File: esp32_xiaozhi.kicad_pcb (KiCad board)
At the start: 2 copper layers, 99.1 x 99.1 mm, 199 parts, among them J1 FT232RL, J10 Micro_SD_Card, J11 logic_convert, J12 tp, J13 tp, J14 tp, J15 tp, J16 tp, J17 tp, J18 tp, J19 tp, J20 tp, J21 USB_B_Mini, J22 JTAG, J3 USB_B_Mini, J5 Oled SSD1306 128x32, J6 FT232RL, J8 tp, J9 Adafruit ST7789, Q10 FDN306P, Q11 FDN306P, Q12 2N7002, Q13 2N7002, Q14 FDN306P, Q4 Q_NPN_BCE, Q5 Q_NPN_BCE, Q6 2N7002, Q7 Q_NPN_BCE, Q8 Q_NPN_BCE, Q9 2N7002, SW1 SW_Push, SW11 boot, SW3 up, SW4 down, SW5 left, SW6 rigth, SW7 up, SW8 down, U1 ESP32-C6-WROOM-1-N8, U2 ESP32-C6-DEVKITC-1-N8, U3 FT232BM, U4 LM1117DT-3.3, U5 MAX98357A, U6 ER_OLEDM0.91_1x-I2C, U7 TXS0108EPW, U8 93CxxA, U9 LM1117DT-3.3, Y1 Crystal, Y2 Crystal

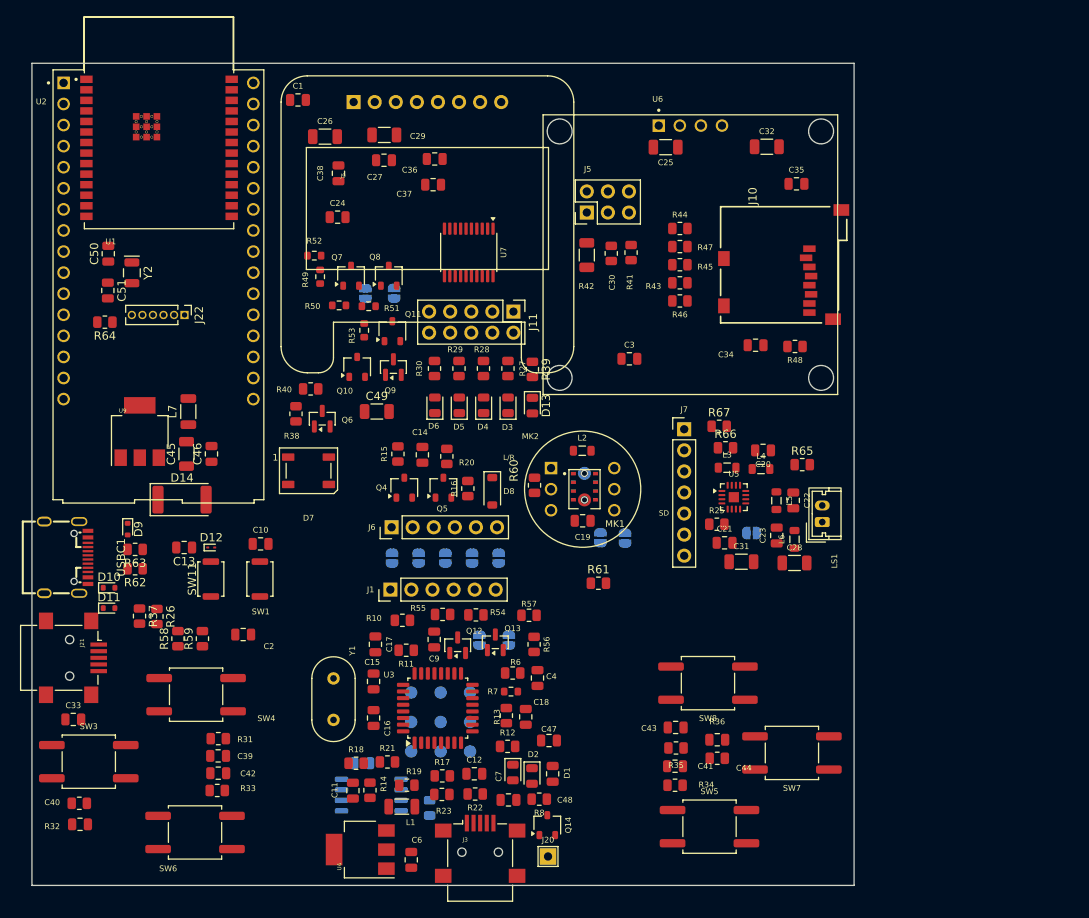
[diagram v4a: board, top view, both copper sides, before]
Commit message: Actualización de esquema y PCB del proyecto ESP32C6 Xiaozhi
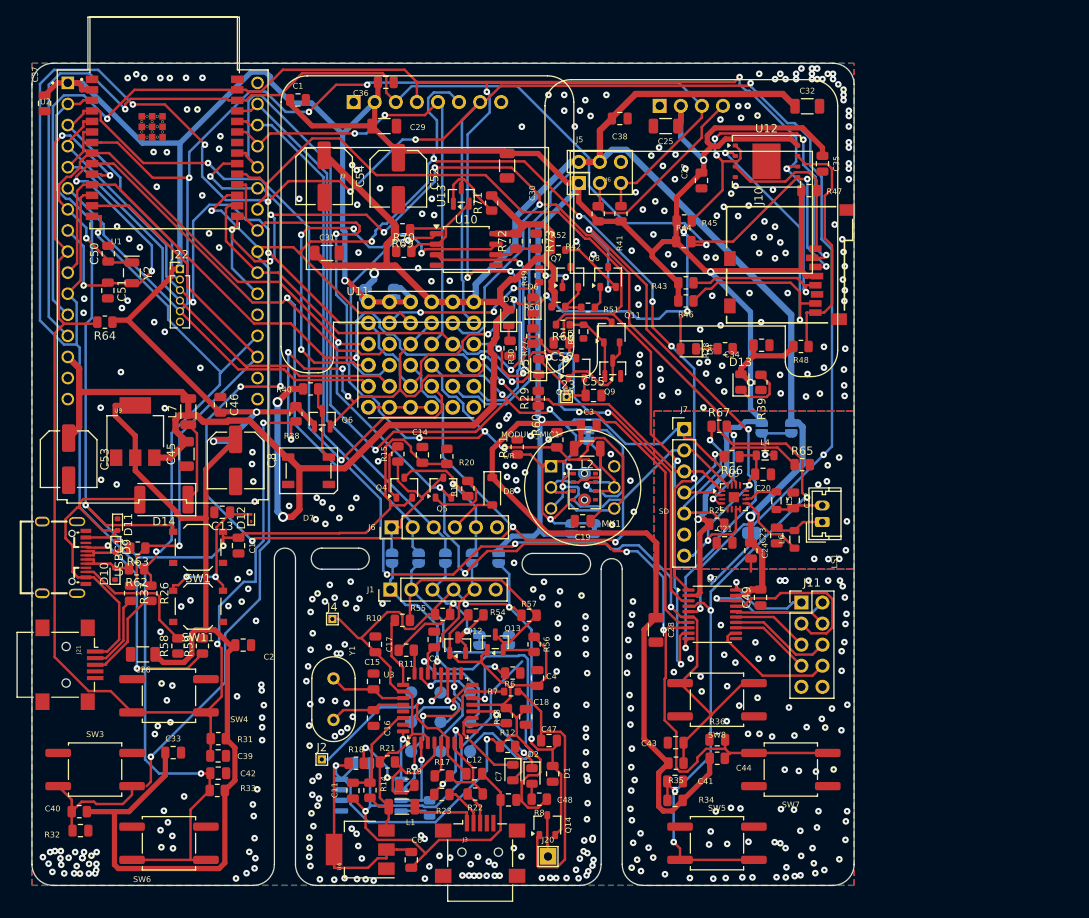
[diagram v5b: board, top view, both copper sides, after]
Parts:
- removed L3: ferrite, Inductor_SMD:L_0805_2012Metric
- added C52: 10uf, Capacitor_SMD:C_Elec_6.3x7.7, F.Cu at (100.0, 67.3)
- added C53: 10uf, Capacitor_SMD:C_Elec_6.3x7.7, F.Cu at (60.3, 101.0)
- added C54: 10uf, Capacitor_SMD:C_Elec_6.3x7.7, F.Cu at (91.1, 67.0)
- added C55: 100nf, Capacitor_SMD:C_0805_2012Metric, F.Cu at (123.5, 93.4)
- added C56: 100nf, Capacitor_SMD:C_0805_2012Metric, F.Cu at (119.7, 87.0)
- added C8: 10uf, Capacitor_SMD:C_Elec_6.3x7.7, F.Cu at (80.4, 101.2)
- added J2: tp_ft232_, TestPoint:TestPoint_THTPad_1.0x1.0mm_Drill0.5mm, F.Cu at (90.8, 137.2)
- added J23: TP_VCC, TestPoint:TestPoint_THTPad_1.0x1.0mm_Drill0.5mm, F.Cu at (120.3, 93.5)
- added J4: tp_ft232_, TestPoint:TestPoint_THTPad_1.0x1.0mm_Drill0.5mm, F.Cu at (92.1, 120.3)
- added JP4: Jumper_2_Open, Jumper:SolderJumper-2_P1.3mm_Bridged_RoundedPad1.0x1.5mm, B.Cu at (122.9, 98.2)
- added JP8: 0, Jumper:SolderJumper-2_P1.3mm_Open_RoundedPad1.0x1.5mm, B.Cu at (147.4, 97.3)
- added JP9: 0, Jumper:SolderJumper-2_P1.3mm_Open_RoundedPad1.0x1.5mm, B.Cu at (143.8, 97.3)
- added R68: 10k, Resistor_SMD:R_0603_1608Metric, F.Cu at (119.8, 84.8)
- added R69: 2k2, Resistor_SMD:R_0805_2012Metric, F.Cu at (100.5, 73.4)
- added R70: 2k2, Resistor_SMD:R_0805_2012Metric, F.Cu at (100.7, 76.0)
- added R71: 0, Resistor_SMD:R_0805_2012Metric, F.Cu at (111.3, 70.2)
- added R72: 2k2, Resistor_SMD:R_0805_2012Metric, F.Cu at (114.2, 74.8)
- added R73: 2k2, Resistor_SMD:R_0805_2012Metric, F.Cu at (116.6, 74.8)
- added U10: LM393, Package_SO:SOIC-8_5.3x5.3mm_P1.27mm, F.Cu at (108.2, 75.8)
- added U11: PIN_HEADER_36, Library:FMINI_PB_6X6, F.Cu at (96.4, 82.1)
- added U12: W25Q128JVE, Package_SON:WSON-8-1EP_8x6mm_P1.27mm_EP3.4x4.3mm, F.Cu at (144.4, 65.2)
- added U13: TL431DBZ, Package_TO_SOT_SMD:SOT-23, F.Cu at (107.6, 69.3)
- C49: footprint Capacitor_SMD:C_1206_3216Metric -> Capacitor_SMD:C_0805_2012Metric
- JP2, JP7: footprint Jumper:SolderJumper-2_P1.3mm_Open_RoundedPad1.0x1.5mm -> Jumper:SolderJumper-2_P1.3mm_Bridged_RoundedPad1.0x1.5mm
- L2: footprint Inductor_SMD:L_0805_2012Metric -> Inductor_SMD:L_1206_3216Metric
- MODULE_MIC1: renamed from MK2; value INMP441ACEZ-R7 -> INMP441_MODULE
- R50, R51, R52: value 10k -> 4k7
- SW1, SW11: footprint Button_Switch_SMD:SW_Push_SPST_NO_Alps_SKRK -> Button_Switch_SMD:SW_Push_1P1T_XKB_TS-1187A
- U6: footprint kiC:LCD_OLED_128X64_1.3_I2C -> kiC:SSD1306_No_Mounting_whitout_Holes
- moved C26 66.1 mm to (69.2, 124.6), turned to 180 degrees
- moved C24 64.0 mm to (142.5, 112.1), turned to -90 degrees
- moved C31 62.3 mm to (91.4, 76.2)
- moved U7 52.6 mm to (137.9, 119.7), turned to 0 degrees
- moved C49 51.4 mm to (143.7, 117.7), turned to 90 degrees
- moved J11 49.3 mm to (148.6, 118.3), turned to 0 degrees
- moved C37 47.8 mm to (57.4, 58.2), turned to -90 degrees
- moved C27 38.3 mm to (136.6, 67.5), turned to -90 degrees
- moved C38 34.5 mm to (126.7, 60.0), turned to 0 degrees
- moved R52 29.4 mm to (119.3, 75.8)
- moved R28 29.2 mm to (139.4, 87.7), turned to 180 degrees
- moved R39 27.6 mm to (143.7, 91.8), turned to 90 degrees
- moved R49 26.4 mm to (117.0, 78.9)
- moved Q10 26.4 mm to (121.5, 90.1)
- moved Q11 26.4 mm to (125.7, 85.8)
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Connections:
- net Net-(J10-DAT1) renamed /micro_sd/PULL_UP2
- C11 pad 2: GND1 -> GND
- C12 pad 2: GND1 -> GND
- C19 pad 2: /inmp441/EN -> VDD_IMP441
- C20 pad 1: GNDA -> GND
- C21 pad 1: GNDA -> GND
- C22 pad 1: GNDA -> GND
- C23 pad 1: GNDA -> GND
- C4 pad 2: GND1 -> GND
- C5 pad 2: GND1 -> GND
- C6 pad 1: GND1 -> GND
- C7 pad 1: GND1 -> GND
- D3 pad 2: /IO_8 -> +5V
- D5 pad 2: /L/R -> /Logic_convert/vcc
- J10 pad 1: CLK_ST7789 -> /micro_sd/PULL_UP1
- J10 pad 3: /MISO -> DI_ST7789
- J10 pad 5: Net-(J10-CLK) -> CLK_ST7789
- J10 pad 7: DI_ST7789 -> /MISO
- J7 pad 6: GNDA -> GND
- JP2 pad 2: /L/R -> /inmp441/L/R
- JP3 pad 1: /L/R -> /inmp441/L/R
- JP7 pad 2: GNDA -> GND
- L2 pad 1: /inmp441/EN -> VDD_IMP441
- L4 pad 2: +5V -> Net-(JP8-A)
- MK1 pad 2: SD -> /SD
- MK1 pad 4: /L/R -> /inmp441/L/R
- MK1 pad 7: /inmp441/EN -> VDD_IMP441
- MK3 pad 2: SD -> /SD
- MK3 pad 4: /L/R -> /inmp441/L/R
- MK3 pad 7: /inmp441/EN -> VDD_IMP441
- MODULE_MIC1 pad 1: /SCK -> /inmp441/L/R
- MODULE_MIC1 pad 2: SD -> /WS
- MODULE_MIC1 pad 3: /WS -> /SCK
- MODULE_MIC1 pad 4: /L/R -> /SD
- MODULE_MIC1 pad 5: GND -> VDD_IMP441
- Q11 pad 1: /OE -> /Logic_convert/CONTROL
- Q9 pad 1: /OE -> /Logic_convert/CONTROL
- R43 pad 2: Net-(J10-CLK) -> CLK_ST7789
- R44 pad 2: /MISO -> DI_ST7789
- R46 pad 1: DI_ST7789 -> /MISO
- R47 pad 2: CLK_ST7789 -> /micro_sd/PULL_UP1
- R50 pad 2: +3V3 -> +5V
- R52 pad 2: +3V3 -> +5V
- R53 pad 2: /OE -> /Logic_convert/CONTROL
- R60 pad 1: SD -> /SD
- R61 pad 1: /L/R -> /inmp441/L/R
- R65 pad 2: GNDA -> GND
- U1 pad 18: SD -> /SD
- U1 pad 19: /L/R -> /IO_21
- U2 pad J3_7: /L/R -> /IO_21
- U2 pad J3_8: SD -> /SD
- U5 pad 11: GNDA -> GND
- U5 pad 15: GNDA -> GND
- U5 pad 17: GNDA -> GND
- U5 pad 3: GNDA -> GND
- U7 pad 9: /Logic_convert/A8 -> /IO_21
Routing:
- net +3V3: track 0.00 -> 623.6 mm, vias 0 -> 8
- net BLK_ST7789: track 0.00 -> 344.1 mm, vias 0 -> 9
- net +5V: track 0.00 -> 322.3 mm, vias 0 -> 4
- net /IO_8: track 0.00 -> 259.5 mm, vias 0 -> 12
- net DC_ST7789: track 0.00 -> 229.7 mm, vias 0 -> 8
- net CLK_ST7789: track 0.00 -> 215.9 mm, vias 0 -> 7
- net /IO_9: track 0.00 -> 206.4 mm, vias 0 -> 10
- net DI_ST7789: track 0.00 -> 201.1 mm, vias 0 -> 4
- net /IO_1: track 0.00 -> 193.4 mm, vias 0 -> 7
- net /CS: track 0.00 -> 182.2 mm, vias 0 -> 11
- net /IO_0: track 0.00 -> 176.1 mm, vias 0 -> 6
- net /SCK: track 0.00 -> 171.4 mm, vias 0 -> 7
- net /SCL_I2C: track 0.00 -> 165.6 mm, vias 0 -> 3
- net /MISO: track 0.00 -> 153.0 mm, vias 0 -> 4
- net /WS: track 0.00 -> 137.7 mm, vias 0 -> 3
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- added copper zone on B.Cu, net (none)
- added copper zone on F.Cu, net (none)
- added copper zone on B.Cu, net GND
- added copper zone on F.Cu, net GND
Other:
- outline, holes or cut-outs redrawn

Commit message: Actualizaciones para versión single ESP32C6
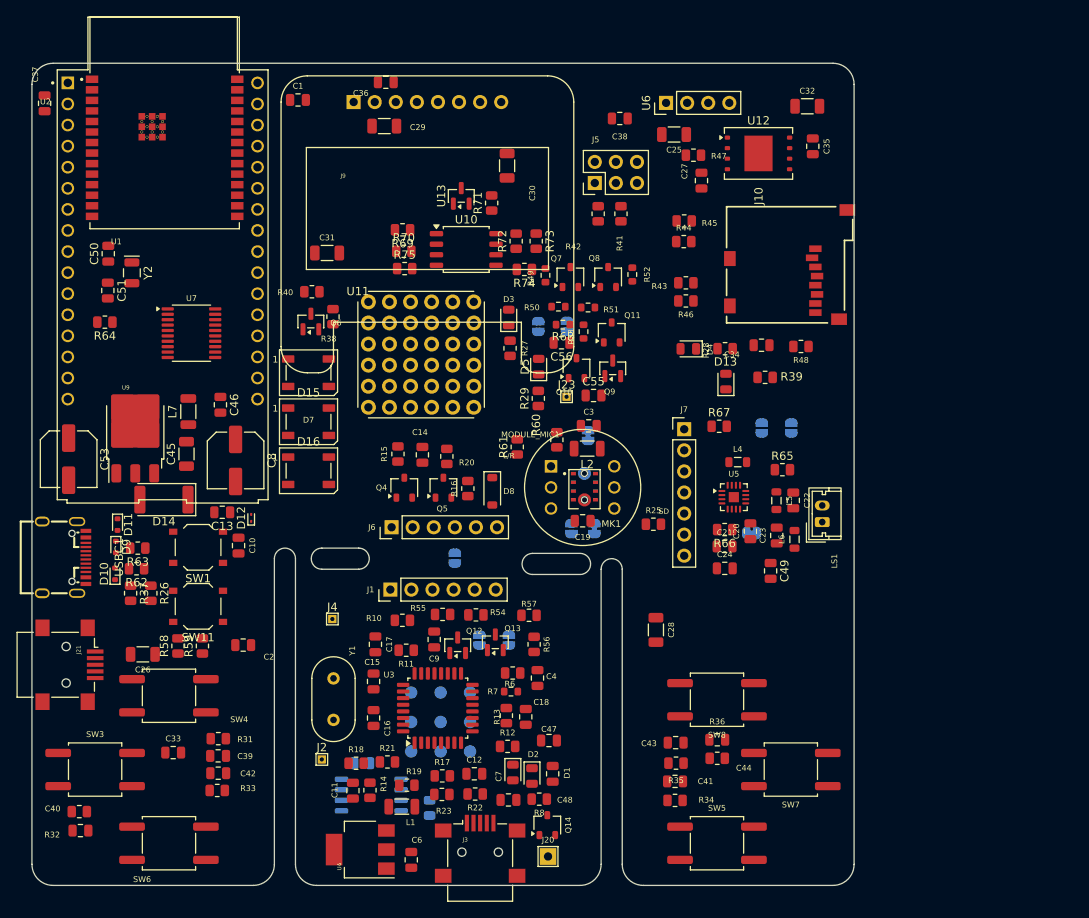
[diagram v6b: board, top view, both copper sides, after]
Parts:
- removed C52, C54: 10uf, Capacitor_SMD:C_Elec_6.3x7.7
- removed D6: LED, Diode_SMD:D_0805_2012Metric
- removed J11: logic_convert, Connector_PinHeader_2.54mm:PinHeader_2x05_P2.54mm_Vertical
- removed J22: JTAG, Connector_PinHeader_1.27mm:PinHeader_1x06_P1.27mm_Vertical
- removed JP10, JP11, JP12, JP13: Jumper_Open, Jumper:SolderJumper-2_P1.3mm_Open_RoundedPad1.0x1.5mm
- removed R30: 2k2, Resistor_SMD:R_0805_2012Metric
- added D15: WS2812B, LED_SMD:LED_WS2812B_PLCC4_5.0x5.0mm_P3.2mm, F.Cu at (89.2, 96.5)
- added D16: WS2812B, LED_SMD:LED_WS2812B_PLCC4_5.0x5.0mm_P3.2mm, F.Cu at (89.2, 102.4)
- added R74: 2k2, Resistor_SMD:R_0805_2012Metric, F.Cu at (115.2, 78.2)
- added R75: 2k2, Resistor_SMD:R_0805_2012Metric, F.Cu at (100.8, 78.1)
- U6: footprint kiC:SSD1306_No_Mounting_whitout_Holes -> Connector_PinHeader_2.54mm:PinHeader_1x04_P2.54mm_Vertical
- U9: footprint kiC:SOT-223-3_TabPin2 -> kiC:TO-252-3_TabPin2
- moved U7 71.3 mm to (75.1, 85.9)
- moved JP5 21.2 mm to (120.3, 85.0)
- moved JP6 21.2 mm to (116.9, 85.1)
- moved R47 14.6 mm to (135.6, 64.4)
- moved R38 12.5 mm to (92.2, 83.9)
- moved D7 11.8 mm to (89.2, 90.6)
- moved Q6 11.8 mm to (89.5, 84.5)
- moved R40 11.7 mm to (89.6, 80.9)
- moved R52 9.37 mm to (128.2, 78.8), turned to 90 degrees
- moved R66 8.83 mm to (139.3, 109.5)
- moved R25 7.64 mm to (130.8, 108.9)
- moved C20 7.03 mm to (142.4, 109.7), turned to 90 degrees
- moved U6 5.85 mm to (132.3, 58.1), turned to 90 degrees
- moved JP14 5.29 mm to (106.8, 113.0)
- moved C24 3.80 mm to (139.4, 114.2), turned to 0 degrees
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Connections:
- C9 pad 2: /ft232/FT_CTS -> /CTS
- D7 pad 2: unconnected-(D7-DOUT-Pad2) -> Net-(D15-DIN)
- J1 pad 1: /ft232/FT_DTR -> /DTR
- J1 pad 2: /ft232/FT_TX -> /MRX
- J1 pad 3: /ft232/FT_RX -> /MTX
- J1 pad 5: /ft232/FT_CTS -> /CTS
- J12 pad 1: /ft232/FT_CTS -> /CTS
- J13 pad 1: /ft232/FT_DTR -> /DTR
- JP15 pad 1: /ft232/FT_RX -> /MTX
- JP15 pad 2: /ft232/FT_RX -> /MTX
- JP16 pad 1: /ft232/FT_TX -> /MRX
- JP16 pad 2: /ft232/FT_TX -> /MRX
- Q12 pad 2: /ft232/FT_RX -> /MTX
- Q12 pad 3: /ft232/FT_RX -> /MTX
- Q13 pad 2: /ft232/FT_TX -> /MRX
- Q13 pad 3: /ft232/FT_TX -> /MRX
- R10 pad 2: /ft232/FT_TX -> /MRX
- R11 pad 2: /ft232/FT_RX -> /MTX
- R54 pad 1: /ft232/FT_RX -> /MTX
- R55 pad 1: /ft232/FT_RX -> /MTX
- R56 pad 1: /ft232/FT_TX -> /MRX
- R57 pad 1: /ft232/FT_TX -> /MRX
- U10 pad 3: /board/IN1+ -> Net-(U10A-+)
- U11 pad 10: /IO_8 -> /B_1
- U11 pad 11: /IO_9 -> /B_2
- U11 pad 12: BLK_ST7789 -> /B_3
- U11 pad 13: /IO_0 -> /B_4
- U11 pad 14: /IO_1 -> /B_5
- U11 pad 15: /IO_8 -> /B_6
- U11 pad 16: RES_ST7789 -> /B_7
- U11 pad 17: /IO_18 -> /B_8
- U11 pad 19: /board/OUT2 -> unconnected-(U11-P19-Pad19)
- U11 pad 20: /board/OUT1 -> unconnected-(U11-P20-Pad20)
- U11 pad 21: /SCK -> unconnected-(U11-P21-Pad21)
- U11 pad 22: /SD -> unconnected-(U11-P22-Pad22)
- U11 pad 23: /WS -> unconnected-(U11-P23-Pad23)
- U11 pad 24: /DIN -> unconnected-(U11-P24-Pad24)
- U11 pad 25: /SCL_I2C -> /board/IN1-
- U11 pad 26: /SDA_I2C -> /board/IN2-
- U11 pad 27: /CS -> /board/IN2+
- U11 pad 28: /MISO -> /board/IN1+
- U11 pad 29: DI_ST7789 -> /board/OUT2
- U11 pad 30: CLK_ST7789 -> /board/OUT1
- U11 pad 7: /CS -> unconnected-(U11-P7-Pad7)
- U11 pad 8: /OE -> unconnected-(U11-P8-Pad8)
- U11 pad 9: DC_ST7789 -> unconnected-(U11-P9-Pad9)
- U3 pad 21: /ft232/FT_DTR -> /DTR
- U3 pad 22: /ft232/FT_CTS -> /CTS
- U7 pad 12: /Logic_convert/B8 -> /B_8
- U7 pad 13: /Logic_convert/B7 -> /B_7
- U7 pad 14: /Logic_convert/B6 -> /B_6
- U7 pad 15: /Logic_convert/B5 -> /B_5
- U7 pad 16: /Logic_convert/B4 -> /B_4
- U7 pad 17: /Logic_convert/B3 -> /B_3
- U7 pad 18: /Logic_convert/B2 -> /B_2
- U7 pad 20: /Logic_convert/B1 -> /B_1
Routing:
- net +3V3: track 623.6 -> 0.00 mm, vias 8 -> 0
- net BLK_ST7789: track 344.1 -> 0.00 mm, vias 9 -> 0
- net +5V: track 322.3 -> 0.00 mm, vias 4 -> 0
- net /IO_8: track 259.5 -> 0.00 mm, vias 12 -> 0
- net DC_ST7789: track 229.7 -> 0.00 mm, vias 8 -> 0
- net CLK_ST7789: track 215.9 -> 0.00 mm, vias 7 -> 0
- net /IO_9: track 206.4 -> 0.00 mm, vias 10 -> 0
- net DI_ST7789: track 201.1 -> 0.00 mm, vias 4 -> 0
- net /IO_1: track 193.4 -> 0.00 mm, vias 7 -> 0
- net /CS: track 182.2 -> 0.00 mm, vias 11 -> 0
- net /IO_0: track 176.1 -> 0.00 mm, vias 6 -> 0
- net /SCK: track 171.4 -> 0.00 mm, vias 7 -> 0
- net /SCL_I2C: track 165.6 -> 0.00 mm, vias 3 -> 0
- net /MISO: track 153.0 -> 0.00 mm, vias 4 -> 0
- net /WS: track 137.7 -> 0.00 mm, vias 3 -> 0
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- removed copper zone on B.Cu, net (none)
- removed copper zone on F.Cu, net (none)
- removed copper zone on B.Cu, net GND
- removed copper zone on F.Cu, net GND
